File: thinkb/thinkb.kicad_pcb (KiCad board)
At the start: 2 copper layers, 298.9 x 142.9 mm, 148 parts, among them P1 battery+, P2 battery-, SW1 SW_Push, SW11 SW_Push, SW12 SW_Push, SW13 SW_Push, SW14 SW_Push, SW15 SW_Push, SW16 SW_Push, SW17 SW_Push, SW18 SW_Push, SW19 SW_Push, SW2 SW_Push, SW20 SW_Push, SW21 SW_Push, SW22 SW_Push, SW23 SW_Push, SW24 SW_Push, SW25 SW_Push, SW26 SW_Push, SW27 SW_Push, SW28 SW_Push, SW29 SW_Push, SW3 SW_Push, SW30 SW_Push, SW31 SW_Push, SW32 SW_Push, SW33 SW_Push, SW34 SW_Push, SW35 SW_Push, SW36 SW_Push, SW37 SW_Push, SW38 SW_Push, SW39 SW_Push, SW4 SW_Push, SW40 SW_Push, SW41 SW_Push, SW42 SW_Push, SW43 SW_Push, SW44 SW_Push, SW45 SW_Push, SW46 SW_Push, SW47 SW_Push, SW48 SW_Push, SW49 SW_Push, SW5 SW_Push, SW50 SW_Push, SW51 SW_Push, SW52 SW_Push, SW53 SW_Push, SW54 SW_Push, SW55 SW_Push, SW56 SW_Push, SW57 SW_Push, SW58 SW_Push, SW59 SW_Push, SW6 SW_Push, SW60 SW_Push, SW61 SW_Push, SW62 Reset, SW63 Power, SW7 SW_Push, SW8 SW_Push, SW9 SW_Push

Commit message: Beautified some tracks
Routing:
- net col6: track 326.4 -> 300.1 mm
- net col5: track 239.0 -> 255.5 mm, vias 2 -> 1
- net Net-(D4-Pad2): track 41.9 -> 25.8 mm
- net Net-(D51-Pad2): track 42.1 -> 26.7 mm
- net col7: track 326.2 -> 341.6 mm
- net Net-(D19-Pad2): track 40.4 -> 25.8 mm
- net Net-(D35-Pad2): track 40.4 -> 25.8 mm
- net col0: track 422.6 -> 410.4 mm
- net row5: track 379.9 -> 391.0 mm
- net col2: track 311.1 -> 300.8 mm
- net row3: track 379.2 -> 388.3 mm
- net col1: track 372.1 -> 363.6 mm
- net row7: track 357.4 -> 364.9 mm
- net row6: track 385.2 -> 392.6 mm
- net Net-(D27-Pad2): track 32.7 -> 25.8 mm
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
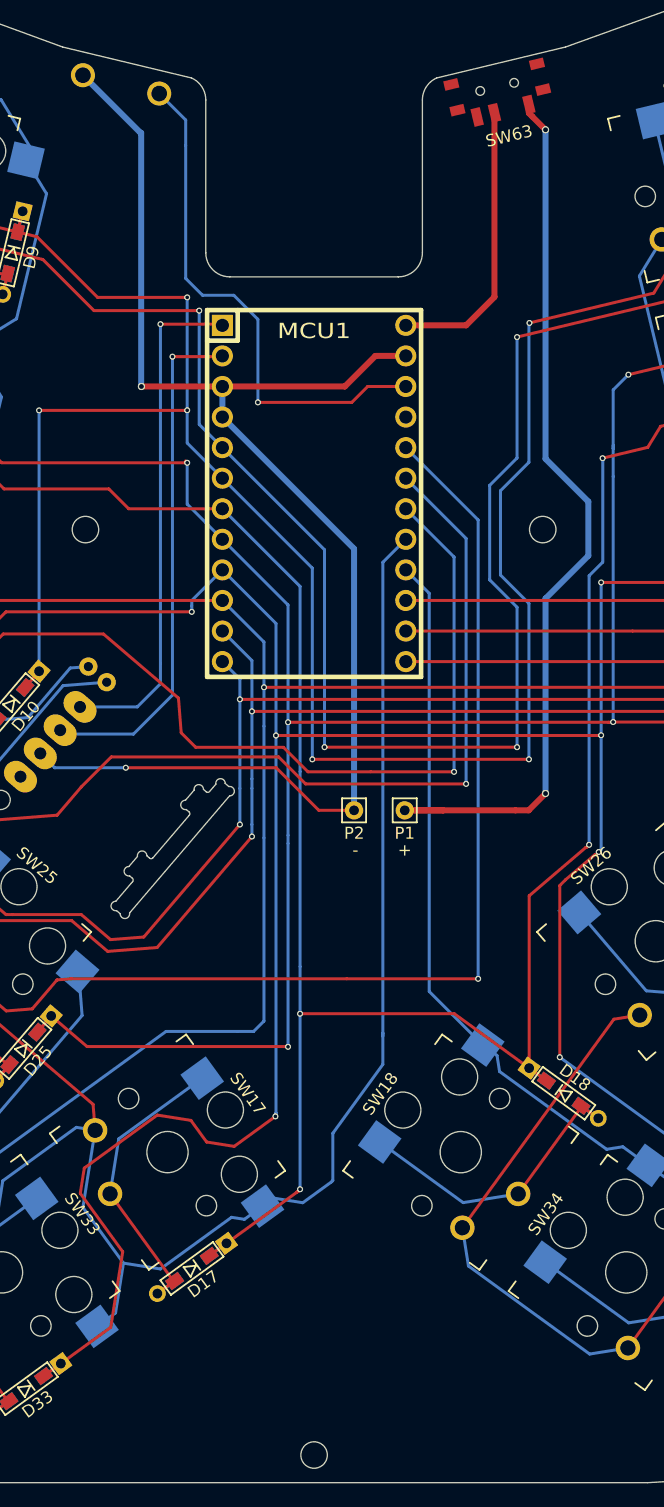
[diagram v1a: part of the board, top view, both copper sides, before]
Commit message: Moving mounting holes
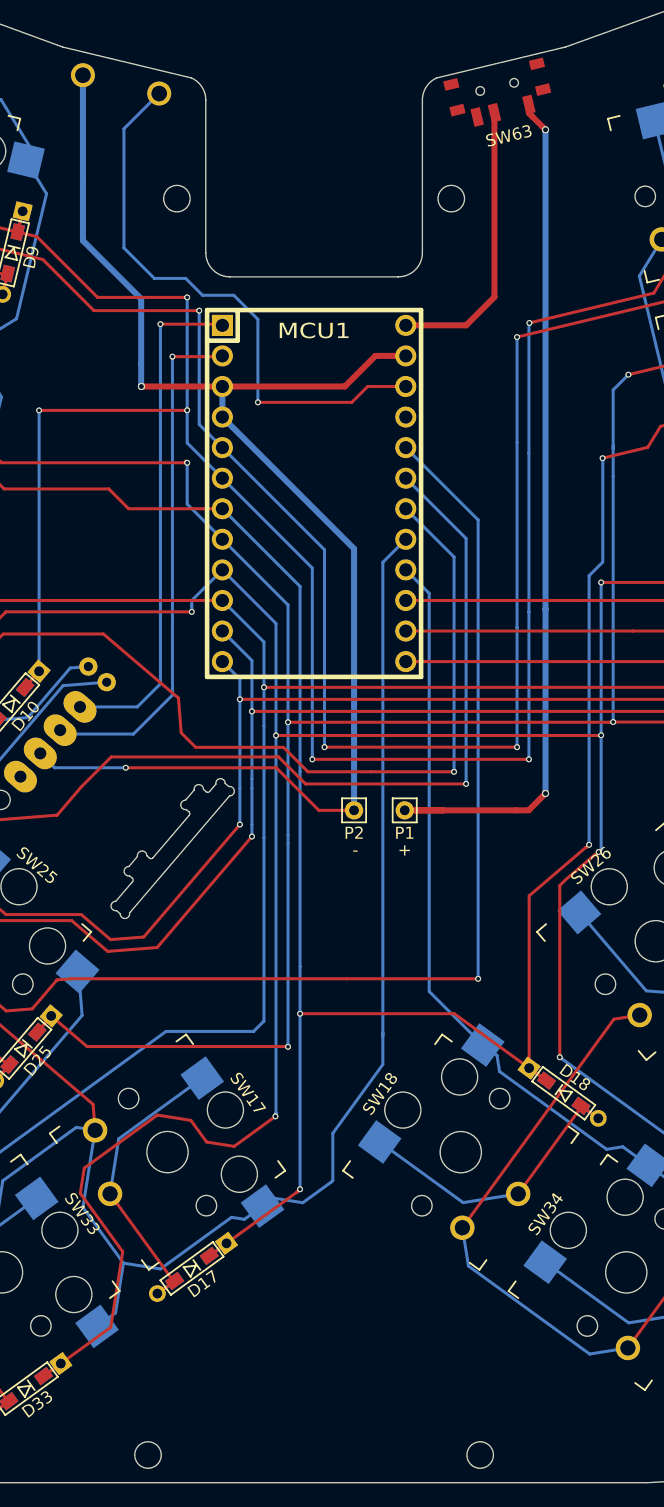
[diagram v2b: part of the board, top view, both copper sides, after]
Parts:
- added H23: MountingHole, MountingHole:MountingHole_2.2mm_M2, F.Cu at (13.8, 79.9)
- moved H10 28.5 mm to (11.4, -24.5)
- moved H6 28.5 mm to (-11.4, -24.5)
- moved H1 13.8 mm to (-13.8, 79.9)
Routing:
- net Net-(MCU1-Pad22): track 43.4 -> 47.4 mm
- net Net-(P1-Pad1): track 76.2 -> 73.2 mm
- net row1: track 381.1 -> 379.1 mm
- net row0: track 356.6 -> 354.7 mm
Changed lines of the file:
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@@
     (thickness 1.6)
     (drawings 65)
-    (tracks 1782)
+    (tracks 1781)
     (zones 0)
-    (modules 148)
+    (modules 149)
     (nets 84)
   )
@@
     (add_net "Net-(D8-Pad2)")
     (add_net "Net-(D9-Pad2)")
+    (add_net "Net-(ENC2-PadNC)")
+    (add_net "Net-(MCU1-Pad21)")
     (add_net "Net-(MCU1-Pad22)")
     (add_net "Net-(MCU1-Pad24)")
     (add_net "Net-(P1-Pad1)")
+    (add_net "Net-(SW63-Pad3)")
     (add_net col0)
     (add_net col1)
@@
     (add_net row7)
   )
+  (module MountingHole:MountingHole_2.2mm_M2 (layer F.Cu)
+    (at 13.8 79.9)
+    (descr "Mounting Hole 2.2mm, no annular, M2")
+    (tags "mounting hole 2.2mm no annular m2")
+    (attr virtual)
+    (fp_text reference H23 (at 0 -3.2) (layer F.SilkS) hide
+      (effects (font (size 1 1) (thickness 0.15)))
+    )
+    (fp_text value MountingHole (at 0 3.2) (layer F.Fab) hide
+      (effects (font (size 1 1) (thickness 0.15)))
+    )
+    (fp_text user %R (at 0.3 0) (layer F.Fab) hide
+      (effects (font (size 1 1) (thickness 0.15)))
+    )
+    (fp_circle (center 0 0) (end 2.2 0) (layer Cmts.User) (width 0.15))
+    (fp_circle (center 0 0) (end 2.45 0) (layer F.CrtYd) (width 0.05))
+    (pad 1 np_thru_hole circle (at 0 0) (size 2.2 2.2) (drill 2.2) (layers *.Cu *.Mask))
+  )
   (module footprints:Kailh_socket_PG1350_optional (layer F.Cu)
     (at -12.181987 54.729609 306)
@@
   )
   (module MountingHole:MountingHole_2.2mm_M2 (layer F.Cu)
-    (at -18.999996 3.000002)
+    (at -11.4 -24.5)
     (descr "Mounting Hole 2.2mm, no annular, M2")
     (tags "mounting hole 2.2mm no annular m2")
@@
   )
   (module MountingHole:MountingHole_2.2mm_M2 (layer F.Cu)
-    (at -0.000001 79.899999)
+    (at -13.8 79.899999)
     (descr "Mounting Hole 2.2mm, no annular, M2")
     (tags "mounting hole 2.2mm no annular m2")
@@
   )
   (module MountingHole:MountingHole_2.2mm_M2 (layer F.Cu)
-    (at 18.999998 3.000002)
+    (at 11.4 -24.5)
     (descr "Mounting Hole 2.2mm, no annular, M2")
     (tags "mounting hole 2.2mm no annular m2")
@@
   (segment (start -9.544291 -15.193738) (end -18.29286 -15.193745) (width 0.25) (layer F.Cu) (net 1))
   (segment (start -35.643094 -22.588987) (end -22.54305 -19.443946) (width 0.25) (layer F.Cu) (net 1))
-  (segment (start 16.864458 -2.948345) (end 16.864442 -12.994825) (width 0.25) (layer B.Cu) (net 1))
-  (segment (start 14.587116 7.174322) (end 14.587107 -0.671008) (width 0.25) (layer B.Cu) (net 1))
-  (segment (start 14.587107 -0.671008) (end 16.864458 -2.948345) (width 0.25) (layer B.Cu) (net 1))
-  (segment (start 16.864454 9.45165) (end 14.587116 7.174322) (width 0.25) (layer B.Cu) (net 1))
-  (segment (start 16.864448 21.079798) (end 16.864454 9.45165) (width 0.25) (layer B.Cu) (net 1))
+  (segment (start 16.864456 11.135544) (end 16.864454 11.135546) (width 0.25) (layer B.Cu) (net 1))
+  (segment (start 16.864456 -4.235544) (end 16.864456 11.135544) (width 0.25) (layer B.Cu) (net 1))
+  (segment (start 16.864448 21.079798) (end 16.864454 11.135546) (width 0.25) (layer B.Cu) (net 1))
+  (segment (start 16.864456 -4.235544) (end 16.864442 -12.994825) (width 0.25) (layer B.Cu) (net 1))
   (segment (start -113.557141 -36.849768) (end -113.971515 -35.123801) (width 0.25) (layer F.Cu) (net 2))
   (segment (start -124.753933 -42.765576) (end -122.333948 -38.816526) (width 0.25) (layer B.Cu) (net 2))
@@
   (segment (start -23.050706 -21.351586) (end -23.086437 -21.351583) (width 0.25) (layer F.Cu) (net 16))
   (segment (start -24.631531 -21.722536) (end -23.086437 -21.351583) (width 0.25) (layer F.Cu) (net 16))
-  (segment (start 17.851762 9.138981) (end 17.851773 22.09248) (width 0.25) (layer B.Cu) (net 16))
-  (segment (start 17.851758 -2.590326) (end 15.487113 -0.225669) (width 0.25) (layer B.Cu) (net 16))
-  (segment (start 15.48712 6.774326) (end 17.851762 9.138981) (width 0.25) (layer B.Cu) (net 16))
-  (segment (start 15.487113 -0.225669) (end 15.48712 6.774326) (width 0.25) (layer B.Cu) (net 16))
-  (segment (start 17.851752 -14.126768) (end 17.851758 -2.590326) (width 0.25) (layer B.Cu) (net 16))
   (segment (start 17.892144 -14.167136) (end 17.851752 -14.126768) (width 0.25) (layer B.Cu) (net 16))
   (segment (start -94.8114 -37.825623) (end -93.753703 -42.231249) (width 0.25) (layer F.Cu) (net 16))
@@
   (segment (start -89.694807 -44.718543) (end -83.071275 -43.128375) (width 0.25) (layer F.Cu) (net 16))
   (segment (start -83.071275 -43.128375) (end -84.917339 -43.571573) (width 0.25) (layer F.Cu) (net 16))
+  (segment (start 17.851758 9.851758) (end 17.851763 9.851763) (width 0.25) (layer B.Cu) (net 16))
+  (segment (start 17.851758 -3.351758) (end 17.851758 9.851758) (width 0.25) (layer B.Cu) (net 16))
+  (segment (start 17.851763 9.851763) (end 17.851773 22.09248) (width 0.25) (layer B.Cu) (net 16))
+  (segment (start 17.851752 -14.126768) (end 17.851758 -3.351758) (width 0.25) (layer B.Cu) (net 16))
   (segment (start -117.525724 -20.319448) (end -117.940077 -18.593503) (width 0.25) (layer F.Cu) (net 17))
   (segment (start -128.722542 -26.23527) (end -126.30254 -22.286231) (width 0.25) (layer B.Cu) (net 17))
@@
   (segment (start 4.451966 -8.890004) (end 7.619996 -8.890003) (width 0.25) (layer F.Cu) (net 81))
   (segment (start 3.131432 -7.569459) (end 4.451966 -8.890004) (width 0.25) (layer F.Cu) (net 81))
+  (segment (start -15.8 -30.302175) (end -12.868883 -33.233292) (width 0.25) (layer B.Cu) (net 81))
+  (segment (start -15.8 -20.4) (end -15.8 -30.302175) (width 0.25) (layer B.Cu) (net 81))
+  (segment (start -4.668569 -7.569442) (end -4.668573 -14.469475) (width 0.25) (layer B.Cu) (net 81))
   (segment (start -4.668573 -14.469475) (end -6.668567 -16.469468) (width 0.25) (layer B.Cu) (net 81))
   (segment (start -6.668567 -16.469468) (end -9.268562 -16.46945) (width 0.25) (layer B.Cu) (net 81))
-  (segment (start -4.668569 -7.569442) (end -4.668573 -14.469475) (width 0.25) (layer B.Cu) (net 81))
+  (segment (start -10.668565 -17.869449) (end -13.269449 -17.869449) (width 0.25) (layer B.Cu) (net 81))
+  (segment (start -13.269449 -17.869449) (end -15.8 -20.4) (width 0.25) (layer B.Cu) (net 81))
   (segment (start -9.268562 -16.46945) (end -10.668565 -17.869449) (width 0.25) (layer B.Cu) (net 81))
-  (segment (start -10.668577 -28.931424) (end -10.668577 -31.032989) (width 0.25) (layer B.Cu) (net 81))
-  (segment (start -10.668577 -31.032989) (end -12.868882 -33.233293) (width 0.25) (layer B.Cu) (net 81))
-  (segment (start -10.668565 -17.869449) (end -10.668577 -28.931424) (width 0.25) (layer B.Cu) (net 81))
   (segment (start -7.620009 -8.889986) (end -7.620009 -6.349998) (width 0.5) (layer B.Cu) (net 82))
   (segment (start -7.620009 -8.889986) (end 2.551985 -8.890008) (width 0.5) (layer F.Cu) (net 82))
@@
   (segment (start -21.557163 22.791543) (end -22.749176 21.599525) (width 0.25) (layer B.Cu) (net 82))
   (segment (start -15.646924 22.791542) (end -21.557163 22.791543) (width 0.25) (layer B.Cu) (net 82))
-  (segment (start -14.421946 -29.968569) (end -14.368569 -29.968568) (width 0.5) (layer B.Cu) (net 82))
-  (segment (start -19.208734 -34.755356) (end -14.421946 -29.968569) (width 0.5) (layer B.Cu) (net 82))
-  (segment (start -14.368568 -8.869446) (end -14.368569 -29.968568) (width 0.5) (layer B.Cu) (net 82))
+  (segment (start -14.368569 -10.731431) (end -14.368569 -16.168569) (width 0.5) (layer B.Cu) (net 82))
+  (segment (start -14.368568 -8.869446) (end -14.368569 -10.731431) (width 0.5) (layer B.Cu) (net 82))
+  (segment (start -19.208735 -21.008735) (end -19.208735 -26.008735) (width 0.5) (layer B.Cu) (net 82))
+  (segment (start -14.368569 -16.168569) (end -19.208735 -21.008735) (width 0.5) (layer B.Cu) (net 82))
+  (segment (start -19.208735 -26.008735) (end -19.208735 -34.755355) (width 0.5) (layer B.Cu) (net 82))
   (segment (start 17.833024 -32.294595) (end 17.847799 -32.318713) (width 0.5) (layer F.Cu) (net 83))
   (via (at 19.23143 24.930539) (size 0.6) (drill 0.4) (layers F.Cu B.Cu) (net 83))
@@
   (segment (start 7.53143 26.330544) (end 10.731424 26.330534) (width 0.5) (layer F.Cu) (net 83))
   (segment (start 10.731424 26.330534) (end 16.73142 26.330542) (width 0.5) (layer F.Cu) (net 83))
-  (segment (start 22.787105 5.174327) (end 19.231435 8.730001) (width 0.5) (layer B.Cu) (net 83))
-  (segment (start 19.231435 8.730001) (end 19.23143 24.930539) (width 0.5) (layer B.Cu) (net 83))
-  (segment (start 22.787115 0.674318) (end 22.787105 5.174327) (width 0.5) (layer B.Cu) (net 83))
-  (segment (start 19.231424 -2.881355) (end 22.787115 0.674318) (width 0.5) (layer B.Cu) (net 83))
   (segment (start 19.231425 -30.219459) (end 19.231425 -30.219459) (width 0.5) (layer B.Cu) (net 83))
-  (segment (start 19.231425 -30.219459) (end 19.231424 -2.881355) (width 0.5) (layer B.Cu) (net 83))
   (via (at 19.231425 -30.219459) (size 0.6) (drill 0.4) (layers F.Cu B.Cu) (net 83))
   (segment (start 18.125441 -31.325443) (end 19.231425 -30.219459) (width 0.5) (layer F.Cu) (net 83))
   (segment (start 17.847806 -31.603078) (end 18.125441 -31.325443) (width 0.5) (layer F.Cu) (net 83))
   (segment (start 17.847806 -32.318719) (end 17.847806 -31.603078) (width 0.5) (layer F.Cu) (net 83))
+  (segment (start 19.231435 9.631435) (end 19.23143 24.930539) (width 0.5) (layer B.Cu) (net 83))
+  (segment (start 19.231424 9.631424) (end 19.231435 9.631435) (width 0.5) (layer B.Cu) (net 83))
+  (segment (start 19.231425 -30.219459) (end 19.231424 9.631424) (width 0.5) (layer B.Cu) (net 83))
 )
